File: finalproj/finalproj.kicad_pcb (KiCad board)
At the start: 2 copper layers, 24 parts, among them J5 Stepper_Motor_Controller, U5 L298N

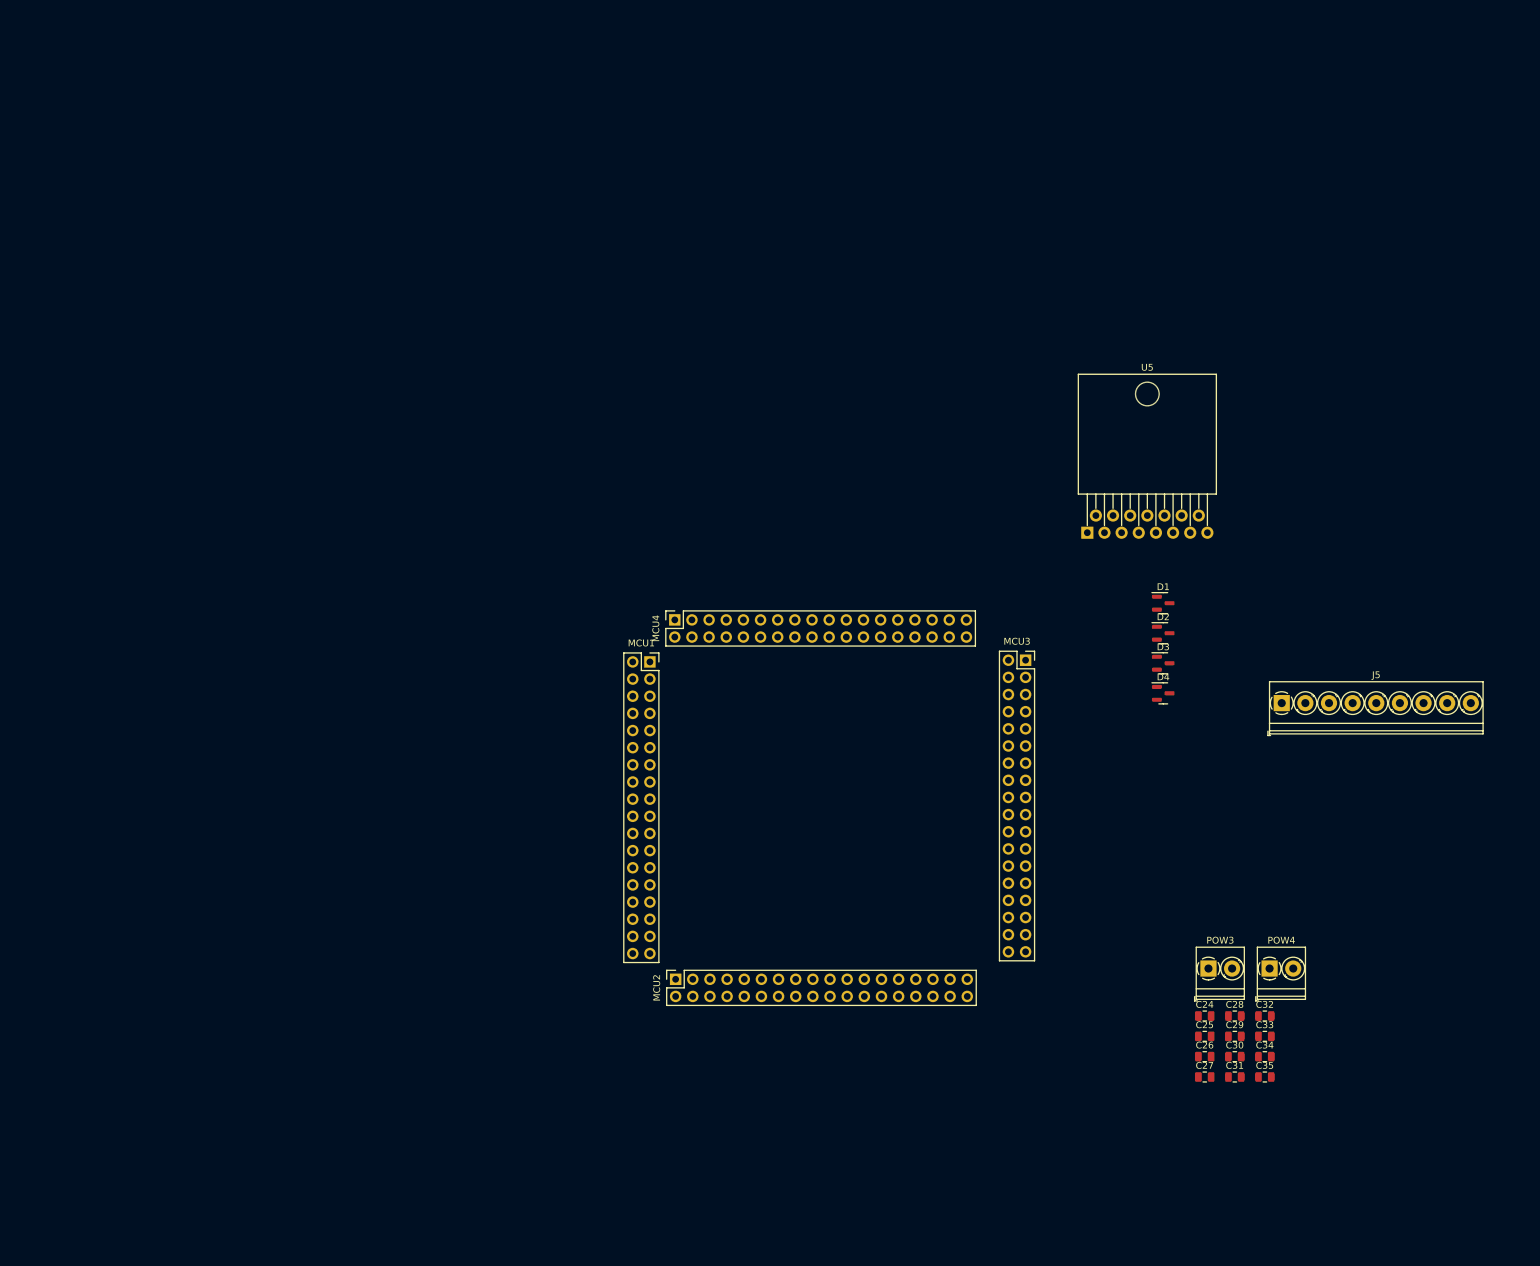
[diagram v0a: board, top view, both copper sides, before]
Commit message: finished schematic with sockets\n initial pcb
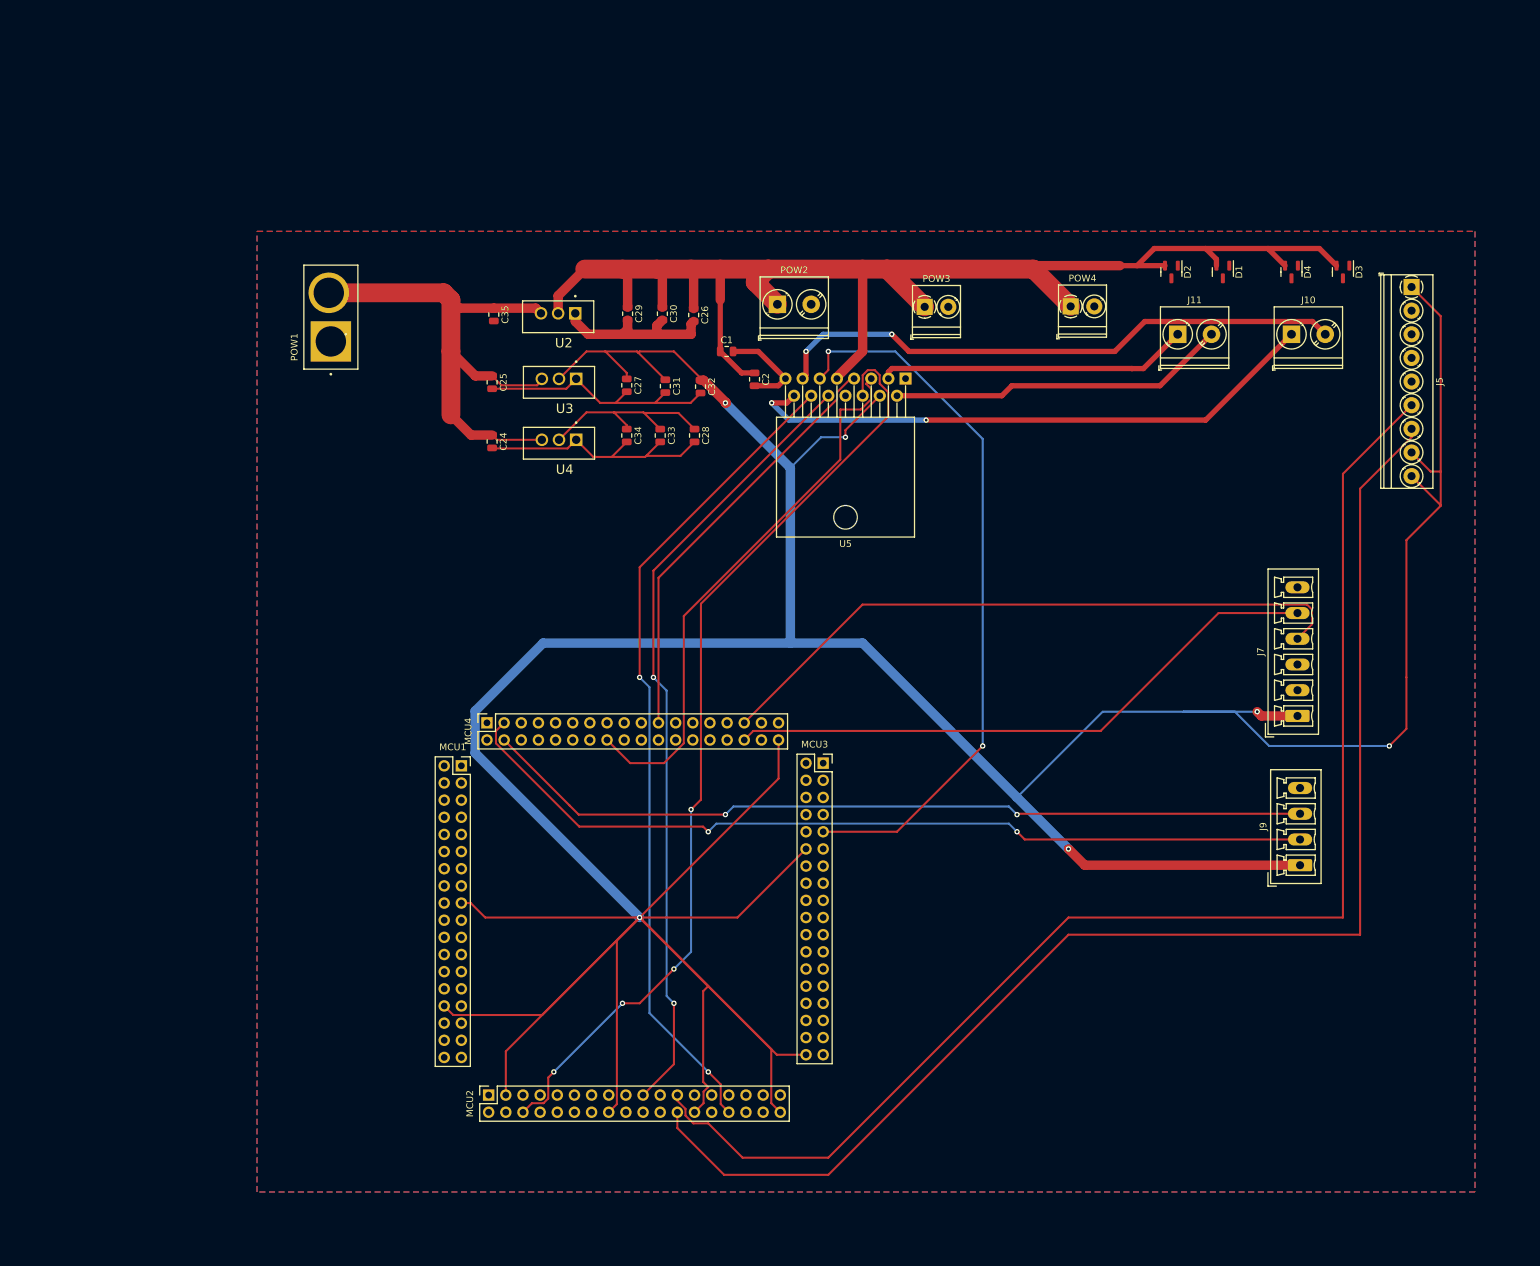
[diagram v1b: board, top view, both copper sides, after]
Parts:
- added C1: 100 nF, Capacitor_SMD:C_0805_2012Metric, F.Cu at (102.5, 38.1)
- added C2: 100 nF, Capacitor_SMD:C_0805_2012Metric, F.Cu at (106.7, 42.2)
- added J10: Motor Out B, TerminalBlock_Phoenix:TerminalBlock_Phoenix_PT-1,5-2-5.0-H_1x02_P5.00mm_Horizontal, F.Cu at (186.2, 35.6)
- added J11: Motor Out A, TerminalBlock_Phoenix:TerminalBlock_Phoenix_PT-1,5-2-5.0-H_1x02_P5.00mm_Horizontal, F.Cu at (169.3, 35.6)
- added J7: LIDAR_Connector, Connector_Phoenix_MC:PhoenixContact_MCV_1,5_6-G-3.81_1x06_P3.81mm_Vertical, F.Cu at (187.1, 92.1)
- added J9: RPI_UART_Conn, Connector_Phoenix_MC:PhoenixContact_MCV_1,5_4-G-3.81_1x04_P3.81mm_Vertical, F.Cu at (187.5, 114.2)
- added POW1: POWER_IN, XT60_YELLOW:AMASS_XT60PB-M, F.Cu at (43.9, 33.0)
- added POW2: Kinect_Power _Connector, TerminalBlock_Phoenix:TerminalBlock_Phoenix_PT-1,5-2-5.0-H_1x02_P5.00mm_Horizontal, F.Cu at (110.1, 31.1)
- added U2: LM1085-12, LM1085IT-5.0:TO254P1054X470X1955-3, F.Cu at (77.6, 32.5)
- added U3: LM1085-5.0, LM1085IT-5.0:TO254P1054X470X1955-3, F.Cu at (77.7, 42.2)
- added U4: LM1085-3.3, LM1085IT-5.0:TO254P1054X470X1955-3, F.Cu at (77.7, 51.2)
- moved C35 160.6 mm to (68.1, 32.6), turned to -90 degrees
- moved C25 143.2 mm to (67.8, 42.7), turned to -90 degrees
- moved C29 139.8 mm to (87.9, 32.5), turned to -90 degrees
- moved C30 138.9 mm to (93.0, 32.5), turned to -90 degrees
- moved C24 135.5 mm to (67.8, 51.4), turned to -90 degrees
- moved C27 133.5 mm to (87.8, 43.1), turned to -90 degrees
- moved C26 133.4 mm to (97.7, 32.7), turned to -90 degrees
- moved C31 132.6 mm to (93.5, 43.2), turned to -90 degrees
- moved C34 131.9 mm to (87.8, 50.5), turned to -90 degrees
- moved C33 126.2 mm to (92.7, 50.5), turned to -90 degrees
- moved C32 125.2 mm to (98.7, 43.3), turned to -90 degrees
- moved C28 117.4 mm to (97.8, 50.5), turned to -90 degrees
- moved POW3 106.6 mm to (131.9, 31.5)
- moved POW4 102.4 mm to (153.5, 31.4)
- moved D4 65.2 mm to (186.2, 26.3), turned to -90 degrees
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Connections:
- net /MotorAOut1 renamed MotorAOut1
- net /MotorAOut2 renamed MotorAOut2
- net /MotorBOut1 renamed MotorBOut1
- net /MotorBOut2 renamed MotorBOut2
- C24 pad 2: GND -> VSS
- C25 pad 1: Net-(U4-VI) -> Net-(POW1-Pin_2)
- C25 pad 2: GND -> VSS
- C26 pad 2: GND -> VSS
- C27 pad 1: +5V -> VDD
- C27 pad 2: GND -> VSS
- C28 pad 2: GND -> VSS
- C29 pad 2: GND -> VSS
- C30 pad 2: GND -> VSS
- C31 pad 1: +5V -> VDD
- C31 pad 2: GND -> VSS
- C32 pad 1: +5V -> VDD
- C32 pad 2: GND -> VSS
- C33 pad 2: GND -> VSS
- C34 pad 2: GND -> VSS
- C35 pad 2: GND -> VSS
- D1 pad 1: GND -> VSS
- D2 pad 1: GND -> VSS
- D3 pad 1: GND -> VSS
- D4 pad 1: GND -> VSS
- J5 pad 1: +5V -> VDD
- J5 pad 2: Net-(J5-GND) -> VSS
- J5 pad 6: /STEP_DIR -> STEP_DIR
- J5 pad 7: /STEP_PWM -> STEP_PWM
- J5 pad 8: +5V -> VDD
- J5 pad 9: +5V -> VDD
- POW3 pad 2: Net-(J5-GND) -> VSS
- POW4 pad 2: Net-(J5-GND) -> VSS
- U5 pad 1: GND -> VSS
- U5 pad 10: /MotorBIn1 -> MotorBIn1
- U5 pad 11: /MotorBPWM -> MotorBPWM
- U5 pad 12: /MotorBIn2 -> MotorBIn2
- U5 pad 13: /MotorOutB1 -> MotorOutB1
- U5 pad 14: /MotorOutB2 -> MotorOutB2
- U5 pad 15: GND -> VSS
- U5 pad 2: /MotorOutA1 -> MotorOutA1
- U5 pad 3: /MotorOutA2 -> MotorOutA2
- U5 pad 4: +5V -> VDD
- U5 pad 5: /MotorAIn1 -> MotorAIn1
- U5 pad 6: /MotorAPWM -> MotorAPWM
- U5 pad 7: /MotorAIn2 -> MotorAIn2
- U5 pad 8: GND -> VSS
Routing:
- net VDD: track 0.00 -> 740.5 mm, vias 0 -> 6
- net +12V: track 0.00 -> 210.2 mm
- net STEP_PWM: track 0.00 -> 199.1 mm
- net STEP_DIR: track 0.00 -> 198.3 mm
- net MotorAPWM: track 0.00 -> 140.7 mm, vias 0 -> 4
- net RPI_UART_TX: track 0.00 -> 129.5 mm, vias 0 -> 2
- net RPI_UART_RX: track 0.00 -> 123.5 mm, vias 0 -> 2
- net MotorBIn2: track 0.00 -> 122.1 mm, vias 0 -> 2
- net MotorBIn1: track 0.00 -> 117.4 mm, vias 0 -> 2
- net VSS: track 0.00 -> 117.1 mm
- net MotorBPWM: track 0.00 -> 107.1 mm, vias 0 -> 2
- net LIDAR_SCL: track 0.00 -> 96.8 mm
- net LIDAR_SDA: track 0.00 -> 89.7 mm
- net MotorOutB2: track 0.00 -> 87.0 mm, vias 0 -> 2
- net MotorOutB1: track 0.00 -> 85.8 mm, vias 0 -> 2
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- added copper zone on B.Cu, net VSS
- added copper zone on F.Cu, net VSS

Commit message: pcb edits fixed pcb errors
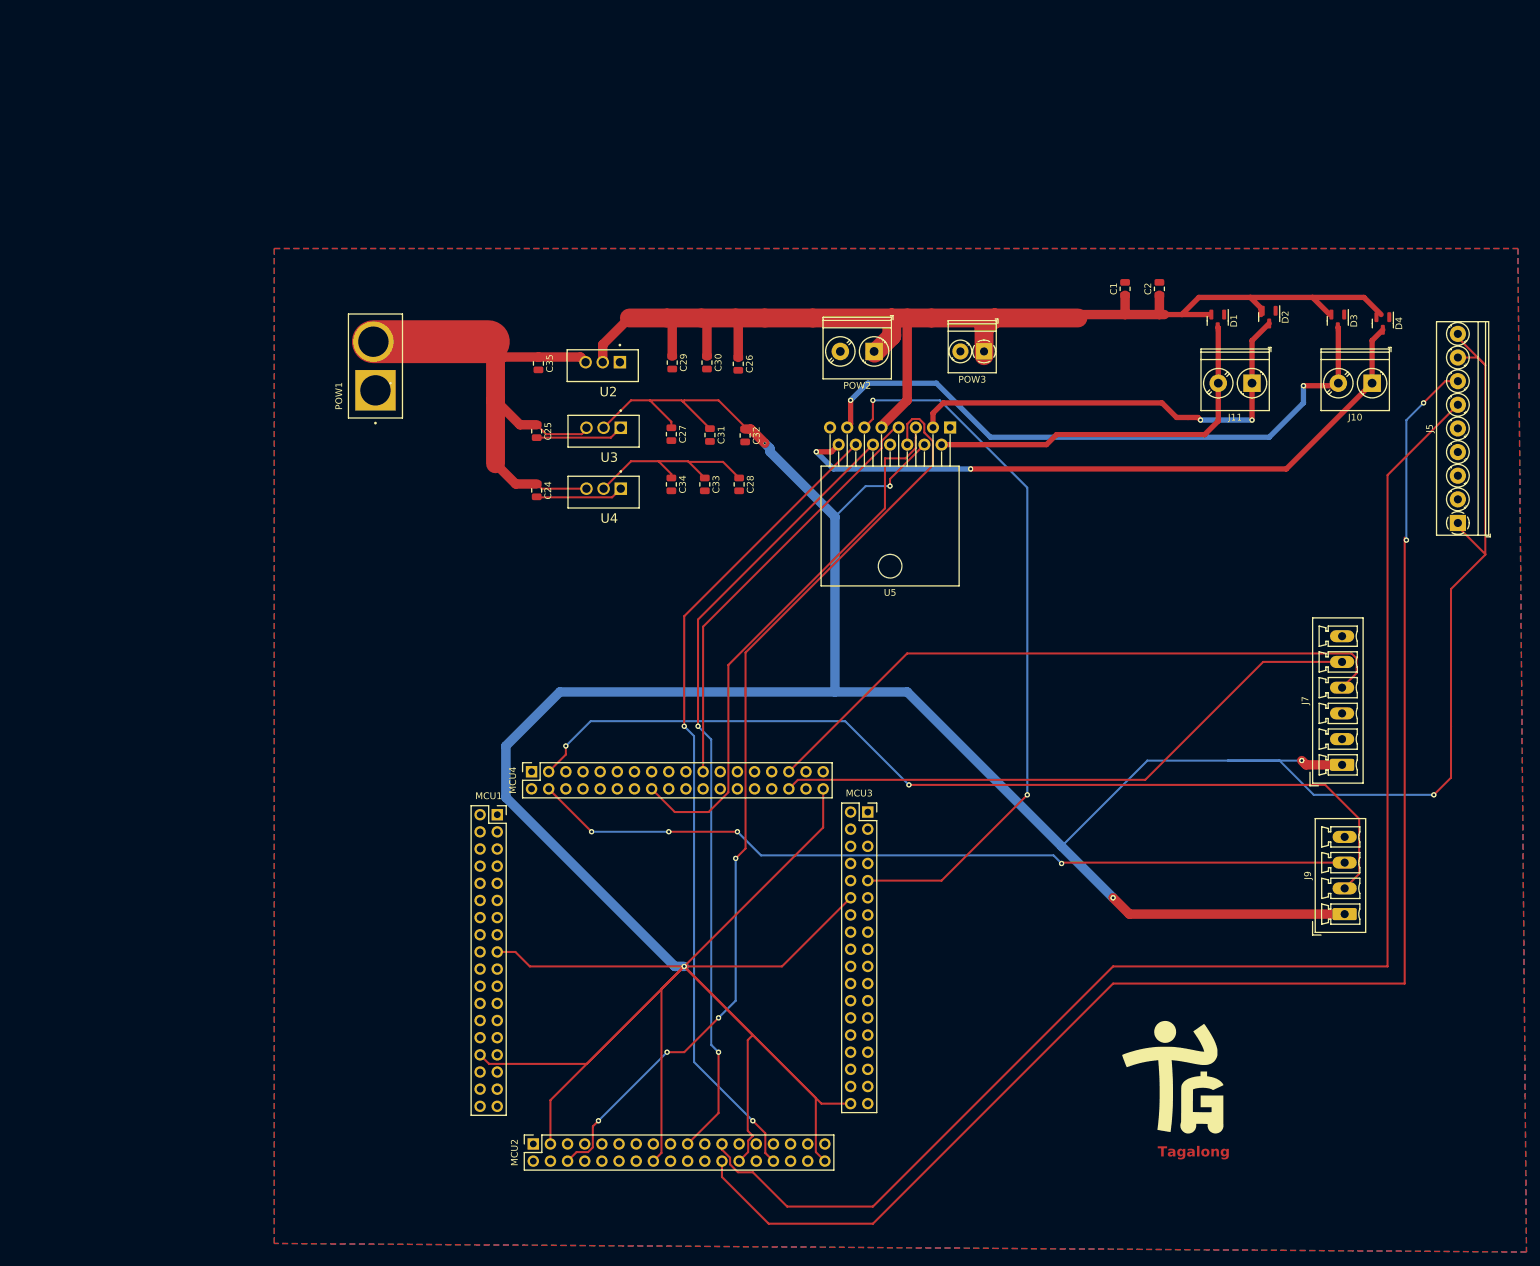
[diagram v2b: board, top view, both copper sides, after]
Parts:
- removed POW4: DC_Motor_Power_Connector, TerminalBlock_Phoenix:TerminalBlock_Phoenix_PT-1,5-2-3.5-H_1x02_P3.50mm_Horizontal
- added G***: LOGO, logos:logo, F.Cu at (170.2, 146.1)
- moved C2 61.4 mm to (166.6, 28.8), turned to 90 degrees
- moved C1 59.7 mm to (161.5, 28.8), turned to 90 degrees
- moved J5 35.6 mm to (210.8, 63.5), turned to 90 degrees
- moved D2 15.9 mm to (182.9, 33.0)
- moved POW2 15.9 mm to (124.4, 38.1), turned to 180 degrees
- moved D4 15.5 mm to (199.7, 34.0)
- moved J10 14.0 mm to (198.1, 42.8), turned to 180 degrees
- moved J11 13.2 mm to (180.3, 42.8), turned to 180 degrees
- moved POW3 11.0 mm to (140.7, 38.1), turned to 180 degrees
- moved J9 9.80 mm to (194.1, 121.4)
- moved C25 9.80 mm to (74.4, 49.9)
- moved C26 9.80 mm to (104.3, 39.9)
- moved C27 9.80 mm to (94.4, 50.4)
- moved MCU2 9.80 mm to (73.9, 155.4)
- moved MCU3 9.80 mm to (123.4, 106.3)
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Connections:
- D1 pad 3: MotorAOut1 -> MotorOutA1
- D2 pad 3: MotorAOut2 -> MotorOutA2
- D3 pad 3: MotorBOut1 -> MotorOutB1
- D4 pad 3: MotorBOut2 -> MotorOutB2
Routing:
- net VSS: track 117.1 -> 26.1 mm
- net +12V: track 210.2 -> 186.7 mm
- net MotorOutA2: track 46.1 -> 66.4 mm, vias 0 -> 2
- net STEP_PWM: track 199.1 -> 215.1 mm, vias 0 -> 2
- net MotorOutB2: track 87.0 -> 100.9 mm
- net RPI_UART_TX: track 129.5 -> 141.0 mm
- net MotorOutB1: track 85.8 -> 93.9 mm
- net STEP_DIR: track 198.3 -> 205.7 mm
- net VDD: track 740.5 -> 746.9 mm
- net MotorOutA1: track 50.3 -> 56.3 mm
- net RPI_UART_RX: track 123.5 -> 122.5 mm, vias 2 -> 4
- net MotorAIn1: track 81.9 -> 81.3 mm
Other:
- board text added: "Tagalong"
